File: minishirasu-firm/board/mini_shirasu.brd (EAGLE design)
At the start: 34 x 50 mm, 74 parts, among them CON1 XT30PW-F, IC2 LMR51606YDBVR, IC3 SN65HVD230DR, J1 SM02B-GHS-TB_LF__SN_, J5 EP2.5-4-SIDE, Q1 FH3406GS, Q2 FH3406GS, Q3 FH3406GS, Q4 FH3406GS, U11 INA2181A1IDGSR, U3 MPQ6528GVE-AEC1-ZQFN-28_MPQ65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, U7 STM32F302_303C2, U9 XC6206, Y1 X322512MSB4SI

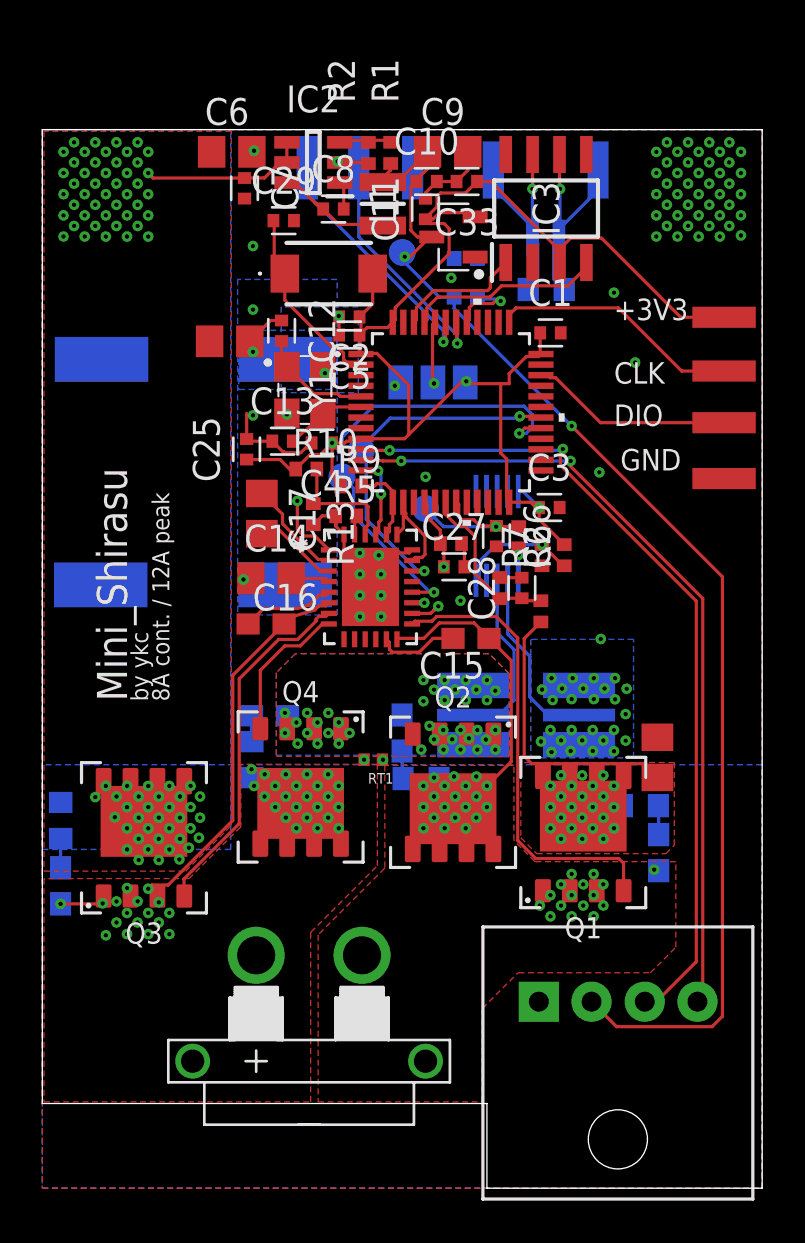
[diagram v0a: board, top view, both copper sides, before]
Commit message: Update mini-shirasu board data to the 2025-12-02 revision
Replace the EAGLE schematic and board, and add the Gerber files
exported on 2025-12-02 under board/gerber/.

Co-Authored-By: Claude Opus 5.5 <noreply@anthropic.com>
Claude-Session: https://claude.ai/code/session_01XNr5i9z8ibucq78UtzMFbR
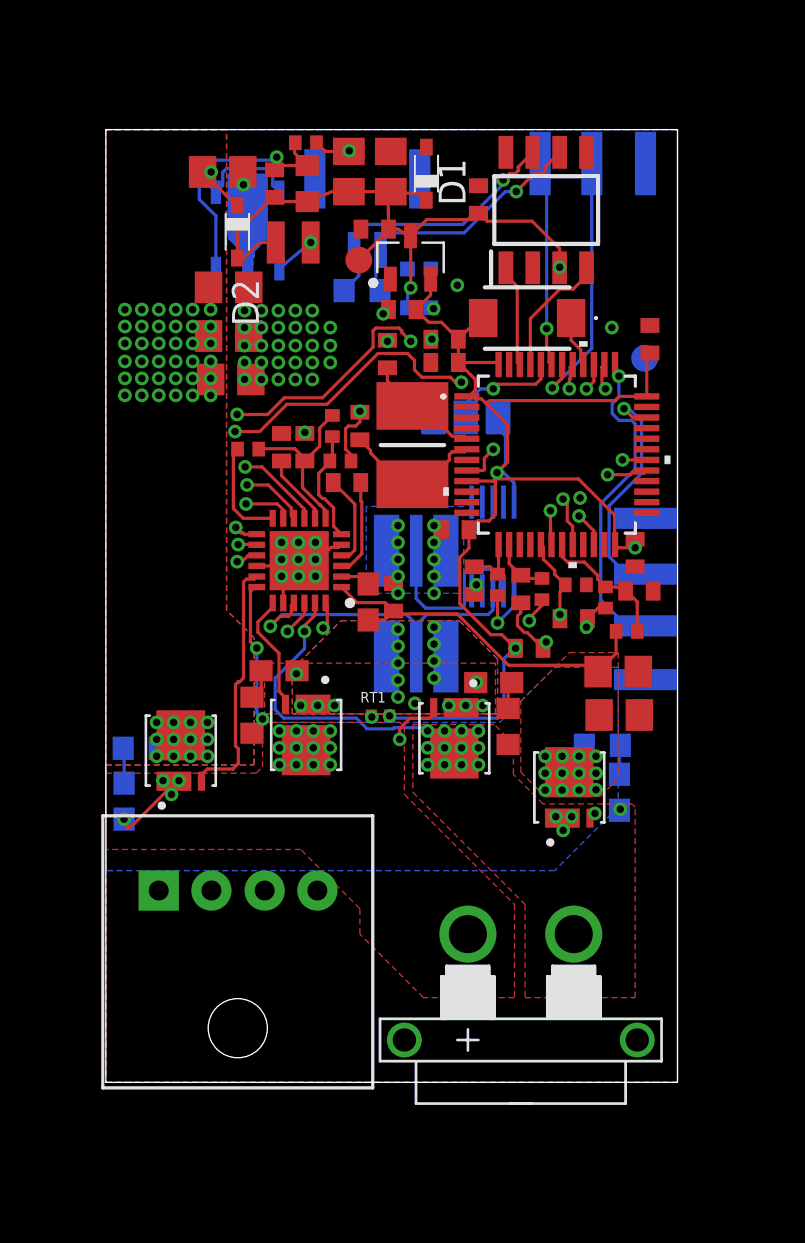
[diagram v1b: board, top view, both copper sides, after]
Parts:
- removed +5V, ISENSE, PWMA, PWMB: TPB1,27, testpad:B1,27
- removed C33: 100n, Capacitor:CAPC1005X60
- removed IC2: LMR51606YDBVR, LMR51606YDBVR:SOT95P280X145-6N
- removed IC3: SN65HVD230DR, SN65HVD230DR:SOT127P600X175-8N
- removed J1: SM02B-GHS-TB_LF__SN_, SM02B-GHS-TB_v2:SM02BGHSTBLFSN
- removed R10: 100k, rcl:R0402
- removed R13, R9: 5.1k, rcl:R0402
- removed U3: MPQ6528GVE-AEC1-ZQFN-28_MPQ6528_MNP, MPQ6528GVE-AEC1-Z:QFN-28_MPQ6528_MNP
- removed Y1: X322512MSB4SI, X322512MSB4SI:X322512MSB4SI
- added C31: 10u, rcl:C0805
- added C43, C44: 6800p, rcl:C0603
- added D1, D2: PMEG6010CEJ,115, nexperia:SOD323_ST
- added IC1: DRV8701PRGER, DRV8701PRGER:QFN50P400X400X100-25N
- added J2: BM02B-GHS-TBT_LF__SN_, BM02B-GHS-TBT_LF__SN_:BM02B-GHS-TBT_1
- added R14: 1k, rcl:R0402
- added TP6, TP8: TPB1,27, testpad:B1,27
- added U1: XC9705B75CPR-GSOT-89-5_TOR-M, CRS_EAGLE_Lib:SOT-89-5_TOR-M
- added U2: TJA1050T_CM,118, TJA1050T_CM_118:SOIC127P600X175-8N
- added Y2: X50328MSB2GI, X50328MSB2GI:RESC5032X135N
- C1, C11, C2, C28, C3: device Capacitor:CAPC1005X60 -> rcl:C0402
- C10: value 1u25V -> 100n; device Capacitor:CAPC1005X60 -> rcl:C0402
- C12: value 33p -> 1u25V; device Capacitor:CAPC1005X60 -> rcl:C0402
- C13: value 33p -> 100n; device Capacitor:CAPC1005X60 -> rcl:C0402
- C14: value 10u -> 10n; device rcl:C0805 -> rcl:C0402
- C15, C16: value 1u -> 1u25V; device rcl:C0603 -> rcl:C0402
- C17: value 470n -> 330p; device rcl:C0805 -> rcl:C0402
- C18: value 220u -> 330p; device Capacitor:CAPAE1030X1050N -> rcl:C0402
- C19: value 10u -> 100n; device rcl:C0805 -> rcl:C0402
- C21: value 6800p -> 10u; device rcl:C0603 -> rcl:C0805
- C22, C23: value 6800p -> 1u25V; device rcl:C0603 -> rcl:C0402
- C24: value 6800p -> 30p; device rcl:C0603 -> rcl:C0402
- C25: value 100n -> 6800p; device Capacitor:CAPC1005X60 -> rcl:C0603
- C26: value 330p -> 6800p; device Capacitor:CAPC1005X60 -> rcl:C0603
- C27: value 1u25V -> 30p; device Capacitor:CAPC1005X60 -> rcl:C0402
- C29: value 100n -> 10u; device Capacitor:CAPC1005X60 -> rcl:C0805
- C30: value 220u -> 10u; device Capacitor:CAPAE1030X1050N -> rcl:C0805
- C4: value 10n -> 100n; device Capacitor:CAPC1005X60 -> rcl:C0402
- C5: value 1u25V -> 2.2u; device Capacitor:CAPC1005X60 -> rcl:C0805
- C6: value 2.2u -> 22u
- C7: value 100n -> 22u; device Capacitor:CAPC1005X60 -> rcl:C0805
- C8: value 100n -> 18p; device Capacitor:CAPC1005X60 -> rcl:C0402
- C9: value 22u -> 1u; device rcl:C0805 -> rcl:C0603
- L1: value DFE252012F-100M=P2 -> 6.8u; device DFE252012F-100M=P2:DFE2HCAH1R0MJ0L -> CRS_EAGLE_Lib:INDUCTOR_1008
- Q1, Q2, Q3, Q4: value FH3406GS -> BSZ042N06NSATMA1; device FH3406GS_PDFN5x6_8L:DFN-8-5X6-FH3406GS -> CRS_EAGLE_Lib:TRANS_BSZ146N10LS5ATMA1
- R1: value 27k -> 120k
- R12: value 2m -> 1m
- R2: value 5.1k -> 680k; device rcl:R0402 -> rcl:R0603
- R5: value 5.1k -> 68k
- R6: value 27k -> 220k
- R7: value 1k -> 20k
- moved C23 31.6 mm to (14.0, 36.5), flipped to the top, turned to 0 degrees
- moved C20 26.9 mm to (5.90, 33.2), turned to 0 degrees
- moved C22 23.8 mm to (12.7, 40.3), flipped to the top, turned to 0 degrees
- moved C9 21.6 mm to (12.4, 22.7), turned to 90 degrees
- moved J5 18.7 mm to (9.99, 9.06)
- moved C24 18.0 mm to (13.3, 34.4), flipped to the top, turned to 270 degrees
- moved C2 17.5 mm to (25.0, 25.0), turned to 90 degrees
- moved C25 16.1 mm to (18.3, 18.9), turned to 0 degrees
- moved C18 15.5 mm to (19.6, 23.3), flipped to the top, turned to 90 degrees
- moved C10 14.7 mm to (11.4, 28.3)
- moved C16 14.5 mm to (22.1, 21.9), turned to 180 degrees
- moved C15 14.2 mm to (16.0, 35.1), turned to 0 degrees
- moved C19 13.5 mm to (17.6, 41.7), turned to 270 degrees
- moved C1 12.9 mm to (25.2, 23.2), turned to 180 degrees
- moved C11 12.6 mm to (9.40, 30.0), turned to 270 degrees
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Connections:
- removed net BST1: C16.1, U3.5
- removed net BST2: C15.2, U3.13
- removed net CB: C8.2, IC2.1
- removed net CPA: C17.1, U3.2
- removed net CPB: C17.2, U3.3
- removed net DT: R5.2, U3.27
- removed net N$2: C12.2, U7.5, Y1.1
- removed net N$3: C13.2, U7.6, Y1.3
- removed net NSLEEP: U3.25, U7.12
- removed net OC_REF: R10.2, R13.1, U3.26
- removed net PWMA: PWMA.TP, U3.20, U7.30
- removed net PWMB: PWMB.TP, U3.18, U7.29
- removed net SW: C8.1, IC2.6, L1.2
- removed net VREG: C14.2, U3.4
- new net APWM: IC1.15, U7.30
- new net AVDD: C11.2, IC1.7, R5.2, R6.2
- new net BPWM: IC1.14, U7.29
- new net CPH: C10.2, IC1.3
- new net CPL: C10.1, IC1.4
- new net DVDD: C12.2, IC1.8
- new net IDRIVE: IC1.12, R5.1
- new net ISENSEA: C18.2, R14.2, U7.14
- new net LX: L1.P$1, U1.1
- new net N$15: C24.2, U7.5, Y2.1
- new net N$20: C27.2, U7.6, Y2.2
- new net OPOUTA: IC1.11, R14.1
- new net SNSOUT: IC1.10, U7.20
- new net VCP: C9.2, IC1.2
- net !EMS: now also IC1.13, U7.22; no longer U3.21, U3.23, U7.14
- net +3V3: now also C14.2, C15.2, C2.2, C23.2, C28.2, C3.2, C4.2, U$1.4; no longer C1.1, C11.1, C2.1, C25.1, C3.1, C33.1, C4.1, C5.1, IC3.3, R10.1, R6.2, R9.1, U$1.1
- net +5V: now also C19.2, C22.2, C6.1, C7.1, C8.1, D1.C, D2.A, L1.P$2, R2.2, TP8.TP, U2.3; no longer +5V.TP, C10.1, C9.1, L1.1, R1.1
- net BUTTON: now also U7.40; no longer C29.1, U7.2
- net CAN_H: now also J2.2, R8.2, U2.7; no longer IC3.7, J1.1, J1.MP1, R8.1
- net CAN_L: now also J2.1, R8.1, U2.6; no longer IC3.6, J1.2, J1.MP2, R8.2
- net CAN_RX: now also U2.4; no longer IC3.4
- net CAN_TX: now also U2.1; no longer IC3.1
- net ENC_A: now also U7.38; no longer U7.10
- net ENC_B: now also U7.39; no longer U7.11
- net FB: now also C8.2, R2.1, U1.3; no longer IC2.3, R2.2
- net GH1: now also IC1.17; no longer U3.7
- net GH2: now also IC1.24; no longer U3.15
- net GL1: now also IC1.19; no longer U3.8
- net GL2: now also IC1.22; no longer U3.16
- net GNDA: now also C1.1, C11.1, C15.1, C16.1, C17.1, C18.1, C19.1, C2.1, C21.2, C22.1, C23.1, C24.1, C27.1, C28.1, C3.1, C31.2, C4.1, D1.A, IC1.16, IC1.20, IC1.25, IC1.5, R1.1, TP6.TP, U$1.1, U1.2, U11.5, U2.2, U2.8; no longer C1.2, C10.2, C11.2, C18.2, C19.2, C2.2, C25.2, C26.2, C27.2, C28.2, C3.2, C33.2, C4.2, C9.2, IC2.2, IC3.2, IC3.8, R13.2, R2.1, R5.1, U$1.4, U11.7, U11.8, U3.19, U3.22, U3.28, U3.29, Y1.2, Y1.4
- net ISENSEB: now also C17.2, U7.13; no longer C26.1, ISENSE.TP, U7.19
- net N$12: now also C25.2; no longer C22.2
- net N$13: now also C26.2; no longer C24.2
- net N$38: now also C44.2; no longer C23.2
- net N$39: now also C43.2; no longer C21.2
- net NFAULT: now also IC1.9, U7.18; no longer R9.2, U3.24, U7.13
- net OUT+: now also C43.1, IC1.23, Q1.1_3, Q2.5_8; no longer C15.1, C21.1, Q1.1, Q1.2, Q1.3, Q2.5, Q2.6, Q2.7, Q2.8, Q2.9, U3.14
- net OUT-: now also C44.1, IC1.18, Q3.1_3, Q4.5_8; no longer C16.2, C23.1, Q3.1, Q3.2, Q3.3, Q4.5, Q4.6, Q4.7, Q4.8, Q4.9, U3.6
- net SP: now also IC1.21
- net TEMP: now also C16.2, U7.17; no longer C27.1, U7.16
- net VCC: now also C13.2, C21.1, C29.1, C31.1, C5.1, C9.1, D2.C, IC1.1, Q1.5_8, Q3.5_8, U1.4, U1.5; no longer C18.1, C19.1, C6.1, C7.1, IC2.4, IC2.5, Q1.5, Q1.6, Q1.7, Q1.8, Q1.9, Q3.5, Q3.6, Q3.7, Q3.8, Q3.9, U3.1
- net VCS: now also C25.1, C26.1, Q2.1_3, Q4.1_3; no longer C22.1, C24.1, Q2.1, Q2.2, Q2.3, Q4.1, Q4.2, Q4.3, U3.17
- net VREF: now also IC1.6; no longer U11.5
- net VSENSE: now also C1.2, U7.19; no longer C28.1, U7.18
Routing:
- net SNSOUT: track 0.00 -> 31.8 mm, vias 0 -> 4
- net +3V3: track 93.0 -> 63.2 mm
- net BPWM: track 0.00 -> 27.5 mm, vias 0 -> 2
- net APWM: track 0.00 -> 27.4 mm, vias 0 -> 2
- net NFAULT: track 3.83 -> 28.5 mm, vias 0 -> 4
- net !EMS: track 4.87 -> 28.0 mm, vias 0 -> 2
- net +5V: track 60.4 -> 83.2 mm
- net PWMB: track 22.5 -> 0.00 mm, vias 2 -> 0
- net OPOUTA: track 0.00 -> 21.3 mm, vias 0 -> 2
- net PWMA: track 17.9 -> 0.00 mm, vias 2 -> 0
- net OUT-: track 21.3 -> 11.2 mm, vias 41 -> 18
- net FB: track 2.58 -> 12.6 mm, vias 0 -> 1
- net VCC: track 35.5 -> 26.7 mm, vias 105 -> 61
- net SP: track 8.22 -> 16.9 mm, vias 0 -> 1
- net AVDD: track 0.00 -> 8.64 mm
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- added copper zone on layer 15, net NONE
- added copper zone on layer 2, net NONE
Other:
- board size 34 x 50 mm -> 27 x 45 mm
- board text removed: "+24V"
- board text removed: "+3V3"
- board text removed: "8A cont. / 12A peak"
- board text removed: "CLK"
- board text removed: "DIO"
- board text removed: "GND"
- board text removed: "Mini_Shirasu"
- board text removed: "PWMA"
- board text removed: "R"
- board text removed: "T"
- board text removed: "by ykc"
